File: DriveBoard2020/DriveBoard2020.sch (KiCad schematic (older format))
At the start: 51 parts

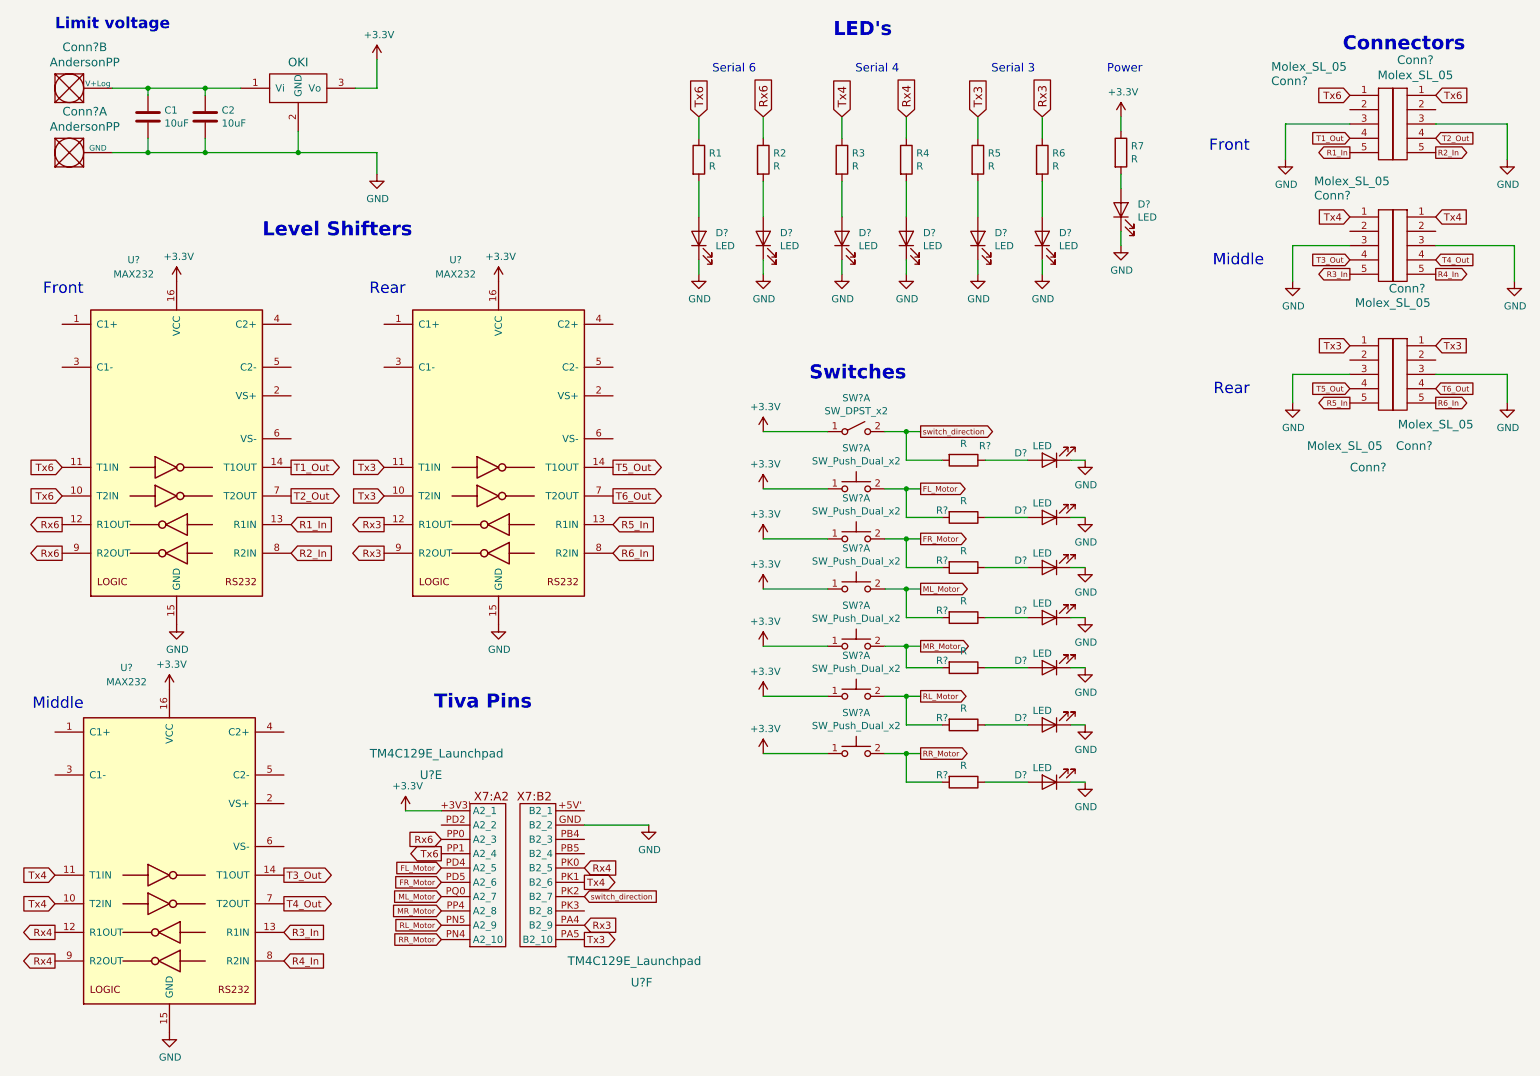
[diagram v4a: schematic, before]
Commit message: Cleaned up schematic, labled and added resistor values
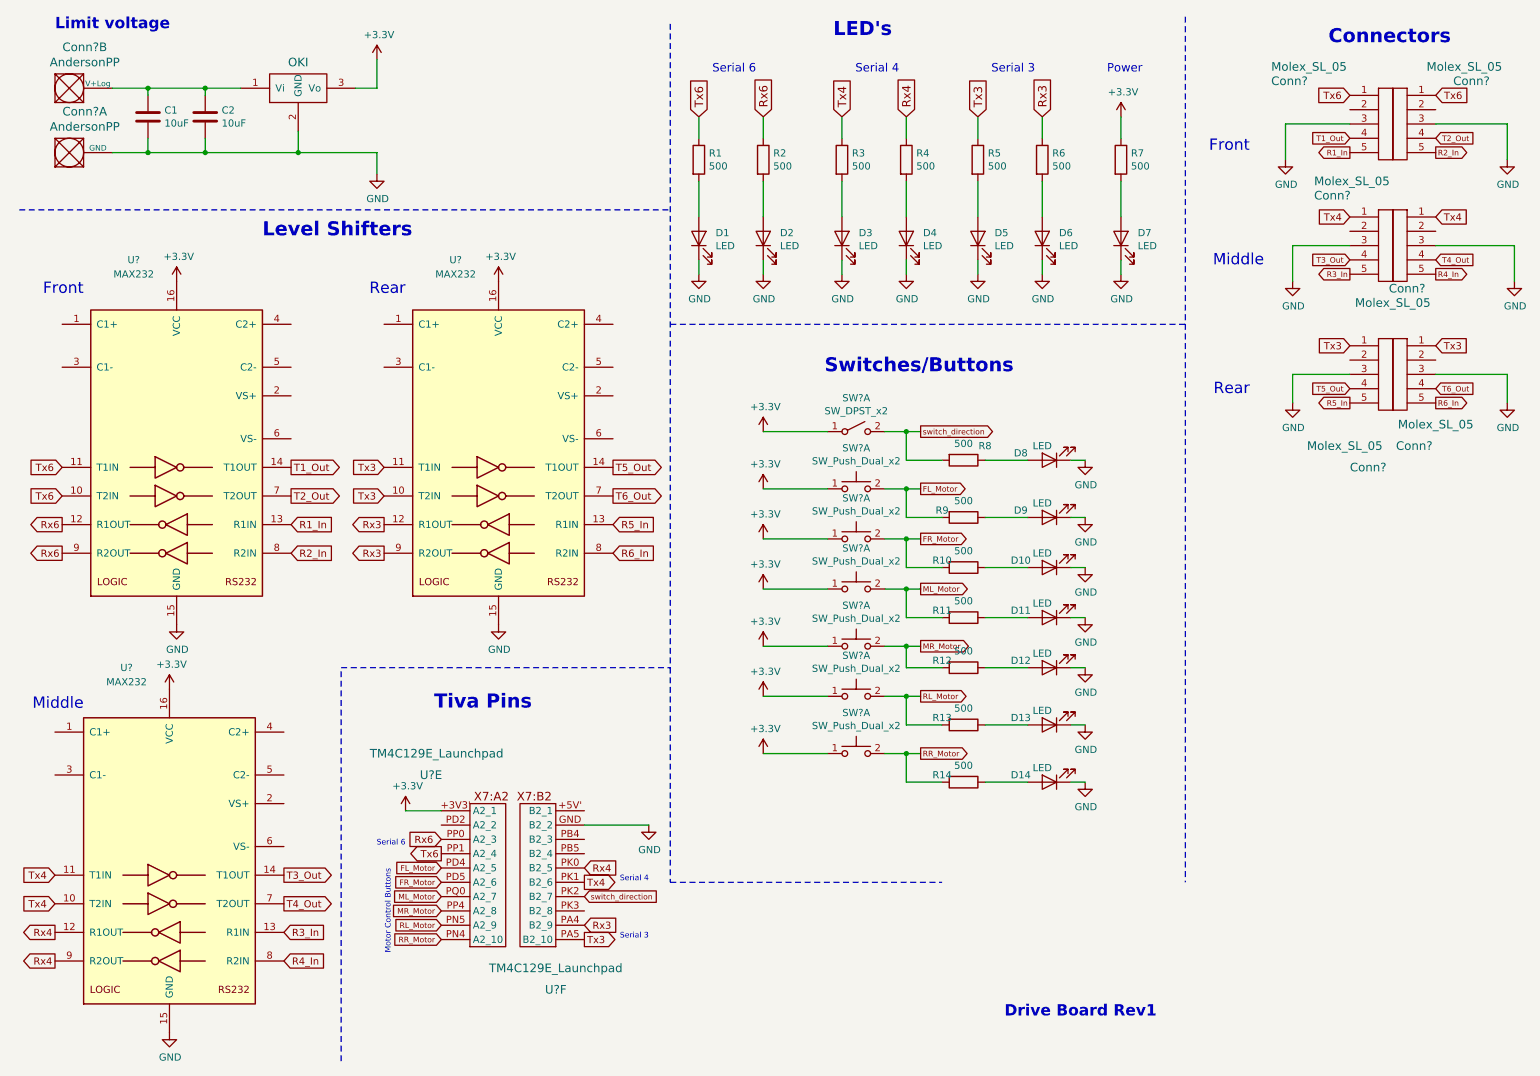
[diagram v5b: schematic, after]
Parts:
- R1, R2, R3, R4, R5, R6, R7: value R -> 500
- R10, R11, R12, R13, R14, R8, R9: renamed from R?; value R -> 500
- gave numbers to parts that had none: 14
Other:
- note added: "Drive Board Rev1"
- note added: "Motor Control Buttons"
- note added: "Switches/Buttons"
- note removed: "Switches"
- moved on the sheet: D7, R7
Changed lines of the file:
@@
 U 6 1 5D9A42ED
 P 4250 7000
-F 0 "U?" H 3650 6750 60  0000 C CNN
-F 1 "TM4C129E_Launchpad" H 3700 6900 60  0000 C CNN
+F 0 "U?" H 4250 6700 60  0000 C CNN
+F 1 "TM4C129E_Launchpad" H 4250 6850 60  0000 C CNN
 F 2 "" H 4250 7000 60  0001 C CNN
 F 3 "" H 4250 7000 60  0001 C CNN
@@
 U 1 1 5DA43D44
 P 10200 1500
-F 0 "Conn?" H 10142 2197 60  0000 C CNN
-F 1 "Molex_SL_05" H 10142 2091 60  0000 C CNN
+F 0 "Conn?" H 9750 2050 60  0000 C CNN
+F 1 "Molex_SL_05" H 9800 2150 60  0000 C CNN
 F 2 "" H 10200 1500 60  0001 C CNN
 F 3 "" H 10200 1500 60  0001 C CNN
@@
 Text GLabel 9800 1050 0    51   Input ~ 0
 Tx6
-Text Notes 9750 750  0    98   ~ 20
+Text Notes 9650 700  0    98   ~ 20
 Connectors
 $Comp
@@
 P 5250 1500
 F 0 "R1" H 5320 1546 50  0000 L CNN
-F 1 "R" H 5320 1455 50  0000 L CNN
+F 1 "500" H 5320 1455 50  0000 L CNN
 F 2 "" V 5180 1500 50  0001 C CNN
 F 3 "~" H 5250 1500 50  0001 C CNN
@@
 	5250 1650 5250 1900
 $Comp
-L Device:LED D?
+L Device:LED D1
 U 1 1 5DAADC37
 P 5250 2050
-F 0 "D?" V 5289 1933 50  0000 R CNN
+F 0 "D1" V 5289 1933 50  0000 R CNN
 F 1 "LED" V 5198 1933 50  0000 R CNN
 F 2 "" H 5250 2050 50  0001 C CNN
@@
 P 5700 1500
 F 0 "R2" H 5770 1546 50  0000 L CNN
-F 1 "R" H 5770 1455 50  0000 L CNN
+F 1 "500" H 5770 1455 50  0000 L CNN
 F 2 "" V 5630 1500 50  0001 C CNN
 F 3 "~" H 5700 1500 50  0001 C CNN
@@
 $EndComp
 $Comp
-L Device:LED D?
+L Device:LED D2
 U 1 1 5DAB09C5
 P 5700 2050
-F 0 "D?" V 5739 1933 50  0000 R CNN
+F 0 "D2" V 5739 1933 50  0000 R CNN
 F 1 "LED" V 5648 1933 50  0000 R CNN
 F 2 "" H 5700 2050 50  0001 C CNN
@@
 P 6250 1500
 F 0 "R3" H 6320 1546 50  0000 L CNN
-F 1 "R" H 6320 1455 50  0000 L CNN
+F 1 "500" H 6320 1455 50  0000 L CNN
 F 2 "" V 6180 1500 50  0001 C CNN
 F 3 "~" H 6250 1500 50  0001 C CNN
@@
 	6250 1650 6250 1900
 $Comp
-L Device:LED D?
+L Device:LED D3
 U 1 1 5DABA283
 P 6250 2050
-F 0 "D?" V 6289 1933 50  0000 R CNN
+F 0 "D3" V 6289 1933 50  0000 R CNN
 F 1 "LED" V 6198 1933 50  0000 R CNN
 F 2 "" H 6250 2050 50  0001 C CNN
@@
 P 6700 1500
 F 0 "R4" H 6770 1546 50  0000 L CNN
-F 1 "R" H 6770 1455 50  0000 L CNN
+F 1 "500" H 6770 1455 50  0000 L CNN
 F 2 "" V 6630 1500 50  0001 C CNN
 F 3 "~" H 6700 1500 50  0001 C CNN
@@
 $EndComp
 $Comp
-L Device:LED D?
+L Device:LED D4
 U 1 1 5DABA297
 P 6700 2050
-F 0 "D?" V 6739 1933 50  0000 R CNN
+F 0 "D4" V 6739 1933 50  0000 R CNN
 F 1 "LED" V 6648 1933 50  0000 R CNN
 F 2 "" H 6700 2050 50  0001 C CNN
@@
 P 7200 1500
 F 0 "R5" H 7270 1546 50  0000 L CNN
-F 1 "R" H 7270 1455 50  0000 L CNN
+F 1 "500" H 7270 1455 50  0000 L CNN
 F 2 "" V 7130 1500 50  0001 C CNN
 F 3 "~" H 7200 1500 50  0001 C CNN
@@
 	7200 1650 7200 1900
 $Comp
-L Device:LED D?
+L Device:LED D5
 U 1 1 5DABE1A4
 P 7200 2050
-F 0 "D?" V 7239 1933 50  0000 R CNN
+F 0 "D5" V 7239 1933 50  0000 R CNN
 F 1 "LED" V 7148 1933 50  0000 R CNN
 F 2 "" H 7200 2050 50  0001 C CNN
@@
 P 7650 1500
 F 0 "R6" H 7720 1546 50  0000 L CNN
-F 1 "R" H 7720 1455 50  0000 L CNN
+F 1 "500" H 7720 1455 50  0000 L CNN
 F 2 "" V 7580 1500 50  0001 C CNN
 F 3 "~" H 7650 1500 50  0001 C CNN
@@
 $EndComp
 $Comp
-L Device:LED D?
+L Device:LED D6
 U 1 1 5DABE1B8
 P 7650 2050
-F 0 "D?" V 7689 1933 50  0000 R CNN
+F 0 "D6" V 7689 1933 50  0000 R CNN
 F 1 "LED" V 7598 1933 50  0000 R CNN
 F 2 "" H 7650 2050 50  0001 C CNN
@@
 L Device:R R7
 U 1 1 5DAC01AD
-P 8200 1450
-F 0 "R7" H 8270 1496 50  0000 L CNN
-F 1 "R" H 8270 1405 50  0000 L CNN
-F 2 "" V 8130 1450 50  0001 C CNN
-F 3 "~" H 8200 1450 50  0001 C CNN
-	1    8200 1450
-	1    0    0    -1
-$EndComp
-Wire Wire Line
-	8200 1200 8200 1300
-$Comp
-L Device:LED D?
+P 8200 1500
+F 0 "R7" H 8270 1546 50  0000 L CNN
+F 1 "500" H 8270 1455 50  0000 L CNN
+F 2 "" V 8130 1500 50  0001 C CNN
+F 3 "~" H 8200 1500 50  0001 C CNN
+	1    8200 1500
+	1    0    0    -1
+$EndComp
+$Comp
+L Device:LED D7
 U 1 1 5DAC1A9F
-P 8200 1850
-F 0 "D?" V 8239 1733 50  0000 R CNN
-F 1 "LED" V 8148 1733 50  0000 R CNN
-F 2 "" H 8200 1850 50  0001 C CNN
-F 3 "~" H 8200 1850 50  0001 C CNN
-	1    8200 1850
+P 8200 2050
+F 0 "D7" V 8239 1933 50  0000 R CNN
+F 1 "LED" V 8148 1933 50  0000 R CNN
+F 2 "" H 8200 2050 50  0001 C CNN
+F 3 "~" H 8200 2050 50  0001 C CNN
+	1    8200 2050
 	0    -1   -1   0
 $EndComp
-Wire Wire Line
-	8200 1600 8200 1700
 $Comp
 L power:GND #PWR?
 U 1 1 5DAC3638
-P 8200 2100
-F 0 "#PWR?" H 8200 1850 50  0001 C CNN
-F 1 "GND" H 8205 1927 50  0000 C CNN
-F 2 "" H 8200 2100 50  0001 C CNN
-F 3 "" H 8200 2100 50  0001 C CNN
-	1    8200 2100
-	1    0    0    -1
-$EndComp
-Wire Wire Line
-	8200 2000 8200 2100
+P 8200 2300
+F 0 "#PWR?" H 8200 2050 50  0001 C CNN
+F 1 "GND" H 8205 2127 50  0000 C CNN
+F 2 "" H 8200 2300 50  0001 C CNN
+F 3 "" H 8200 2300 50  0001 C CNN
+	1    8200 2300
+	1    0    0    -1
+$EndComp
 Text Notes 8350 900  2    59   ~ 0
 Power
-Text Notes 6700 3050 2    98   ~ 20
-Switches
+Text Notes 7450 3000 2    98   ~ 20
+Switches/Buttons
 $Comp
 L Switch:SW_DPST_x2 SW?
@@
 	6700 3400 6800 3400
 $Comp
-L Device:LED D?
+L Device:LED D8
 U 1 1 5DB0DCCD
 P 7700 3600
-F 0 "D?" H 7900 3550 50  0000 C CNN
+F 0 "D8" H 7900 3550 50  0000 C CNN
 F 1 "LED" H 7750 3500 50  0000 C CNN
 F 2 "" H 7700 3600 50  0001 C CNN
@@
 $EndComp
 $Comp
-L Device:R R?
+L Device:R R8
 U 1 1 5DB0FB7A
 P 7100 3600
-F 0 "R?" V 7000 3750 50  0000 C CNN
-F 1 "R" V 6984 3600 50  0000 C CNN
+F 0 "R8" V 7000 3750 50  0000 C CNN
+F 1 "500" V 6984 3600 50  0000 C CNN
 F 2 "" V 7030 3600 50  0001 C CNN
 F 3 "~" H 7100 3600 50  0001 C CNN
@@
 	6700 3800 6800 3800
 $Comp
-L Device:R R?
+L Device:R R9
 U 1 1 5DB14CA8
 P 7100 4000
-F 0 "R?" V 7050 3850 50  0000 C CNN
-F 1 "R" V 6984 4000 50  0000 C CNN
+F 0 "R9" V 7050 3850 50  0000 C CNN
+F 1 "500" V 6984 4000 50  0000 C CNN
 F 2 "" V 7030 4000 50  0001 C CNN
 F 3 "~" H 7100 4000 50  0001 C CNN
@@
 	7250 4000 7550 4000
 $Comp
-L Device:LED D?
+L Device:LED D9
 U 1 1 5DB1AFB8
 P 7700 4000
-F 0 "D?" H 7900 3950 50  0000 C CNN
+F 0 "D9" H 7900 3950 50  0000 C CNN
 F 1 "LED" H 7750 3900 50  0000 C CNN
 F 2 "" H 7700 4000 50  0001 C CNN
@@
 	6700 4150 6800 4150
 $Comp
-L Device:R R?
+L Device:R R10
 U 1 1 5DB1F255
 P 7100 4350
-F 0 "R?" V 7050 4200 50  0000 C CNN
-F 1 "R" V 6984 4350 50  0000 C CNN
+F 0 "R10" V 7050 4200 50  0000 C CNN
+F 1 "500" V 6984 4350 50  0000 C CNN
 F 2 "" V 7030 4350 50  0001 C CNN
 F 3 "~" H 7100 4350 50  0001 C CNN
@@
 	7250 4350 7550 4350
 $Comp
-L Device:LED D?
+L Device:LED D10
 U 1 1 5DB21877
 P 7700 4350
-F 0 "D?" H 7900 4300 50  0000 C CNN
+F 0 "D10" H 7900 4300 50  0000 C CNN
 F 1 "LED" H 7750 4250 50  0000 C CNN
 F 2 "" H 7700 4350 50  0001 C CNN
@@
 	6700 4500 6800 4500
 $Comp
-L Device:R R?
+L Device:R R11
 U 1 1 5DB2408E
 P 7100 4700
-F 0 "R?" V 7050 4550 50  0000 C CNN
-F 1 "R" V 6984 4700 50  0000 C CNN
+F 0 "R11" V 7050 4550 50  0000 C CNN
+F 1 "500" V 6984 4700 50  0000 C CNN
 F 2 "" V 7030 4700 50  0001 C CNN
 F 3 "~" H 7100 4700 50  0001 C CNN
@@
 	7250 4700 7550 4700
 $Comp
-L Device:LED D?
+L Device:LED D11
 U 1 1 5DB26770
 P 7700 4700
-F 0 "D?" H 7900 4650 50  0000 C CNN
+F 0 "D11" H 7900 4650 50  0000 C CNN
 F 1 "LED" H 7750 4600 50  0000 C CNN
 F 2 "" H 7700 4700 50  0001 C CNN
@@
 	6700 4900 6800 4900
 $Comp
-L Device:R R?
+L Device:R R12
 U 1 1 5DB29413
 P 7100 5050
-F 0 "R?" V 7050 4900 50  0000 C CNN
-F 1 "R" V 6984 5050 50  0000 C CNN
+F 0 "R12" V 7050 4900 50  0000 C CNN
+F 1 "500" V 6984 5050 50  0000 C CNN
 F 2 "" V 7030 5050 50  0001 C CNN
 F 3 "~" H 7100 5050 50  0001 C CNN
@@
 	7250 5050 7550 5050
 $Comp
-L Device:LED D?
+L Device:LED D12
 U 1 1 5DB2BE6F
 P 7700 5050
-F 0 "D?" H 7900 5000 50  0000 C CNN
+F 0 "D12" H 7900 5000 50  0000 C CNN
 F 1 "LED" H 7750 4950 50  0000 C CNN
 F 2 "" H 7700 5050 50  0001 C CNN
@@
 	6700 5250 6800 5250
 $Comp
-L Device:R R?
+L Device:R R13
 U 1 1 5DB2EE1B
 P 7100 5450
-F 0 "R?" V 7050 5300 50  0000 C CNN
-F 1 "R" V 6984 5450 50  0000 C CNN
+F 0 "R13" V 7050 5300 50  0000 C CNN
+F 1 "500" V 6984 5450 50  0000 C CNN
 F 2 "" V 7030 5450 50  0001 C CNN
 F 3 "~" H 7100 5450 50  0001 C CNN
@@
 	7250 5450 7550 5450
 $Comp
-L Device:LED D?
+L Device:LED D13
 U 1 1 5DB31B65
 P 7700 5450
-F 0 "D?" H 7900 5400 50  0000 C CNN
+F 0 "D13" H 7900 5400 50  0000 C CNN
 F 1 "LED" H 7750 5350 50  0000 C CNN
 F 2 "" H 7700 5450 50  0001 C CNN
@@
 	6700 5650 6800 5650
 $Comp
-L Device:R R?
+L Device:R R14
 U 1 1 5DB353D4
 P 7100 5850
-F 0 "R?" V 7050 5700 50  0000 C CNN
-F 1 "R" V 6984 5850 50  0000 C CNN
+F 0 "R14" V 7050 5700 50  0000 C CNN
+F 1 "500" V 6984 5850 50  0000 C CNN
 F 2 "" V 7030 5850 50  0001 C CNN
 F 3 "~" H 7100 5850 50  0001 C CNN
@@
 	7250 5850 7550 5850
 $Comp
-L Device:LED D?
+L Device:LED D14
 U 1 1 5DB38360
 P 7700 5850
-F 0 "D?" H 7900 5800 50  0000 C CNN
+F 0 "D14" H 7900 5800 50  0000 C CNN
 F 1 "LED" H 7750 5750 50  0000 C CNN
 F 2 "" H 7700 5850 50  0001 C CNN
@@
 Text GLabel 3450 6950 0    39   Input ~ 0
 RR_Motor
+Text Notes 3200 6300 2    39   ~ 0
+Serial 6
+Text Notes 4900 6550 2    39   ~ 0
+Serial 4
+Text Notes 4900 6950 2    39   ~ 0
+Serial 3
+Text Notes 3100 7050 1    39   ~ 0
+Motor Control Buttons
+Wire Wire Line
+	8200 2200 8200 2300
+Wire Wire Line
+	8200 1200 8200 1350
+Wire Wire Line
+	8200 1650 8200 1900
+Text Notes 8450 7500 2    79   ~ 16
+Drive Board Rev1
+Wire Notes Line style solid
+	2750 7800 2750 5050
+Wire Notes Line style solid
+	2750 5050 5050 5050
+Wire Notes Line style solid
+	500  1850 5050 1850
+Wire Notes Line style solid
+	5050 550  5050 5050
+Wire Notes Line style solid
+	5050 2650 8650 2650
+Wire Notes Line style solid
+	5050 5050 5050 6550
+Wire Notes Line style solid
+	5050 6550 6950 6550
+Wire Notes Line style solid
+	8650 500  8650 6550
 $EndSCHEMATC

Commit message: started assigning footprints
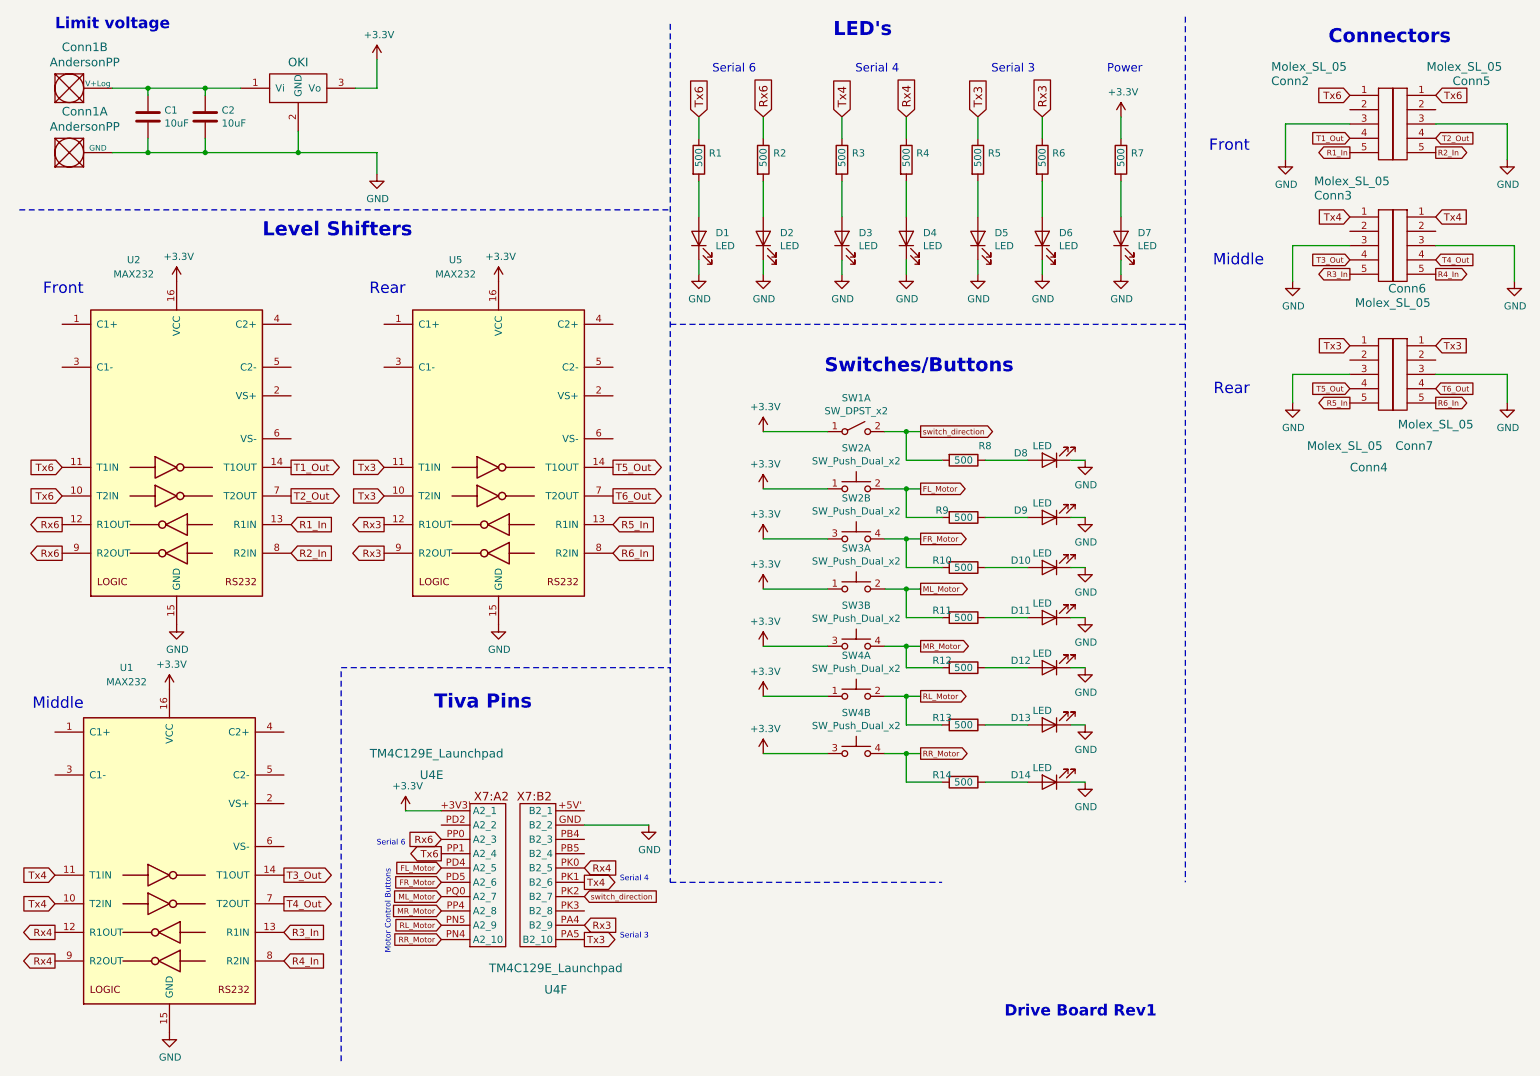
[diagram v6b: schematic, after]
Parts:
- C1, C2: footprint (none) -> Capacitor_SMD:C_0603_1608Metric_Pad1.05x0.95mm_HandSolder
- Conn1: renamed from Conn?; footprint (none) -> MRDT_Connectors:Anderson_2_Horizontal_Side_by_Side
- Conn2, Conn3, Conn4, Conn5, Conn6, Conn7: renamed from Conn?; footprint (none) -> MRDT_Connectors:MOLEX_SL_05_Horizontal
- D1, D10, D11, D12, D13, D14, D2, D3, D4, D5, D6, D7, D8, D9: footprint (none) -> LED_SMD:LED_0603_1608Metric_Pad1.05x0.95mm_HandSolder
- R1, R10, R11, R12, R13, R14, R2, R3, R4, R5, R6, R7, R8, R9: footprint (none) -> Resistor_SMD:R_0603_1608Metric_Pad1.05x0.95mm_HandSolder
- U3: renamed from U?; footprint (none) -> MRDT_Devices:OKI_Horizontal
- gave numbers to parts that had none: 8
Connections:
- net +3V3: now also SW2.3 (C), SW3.3 (C), SW4.3 (C); no longer SW2.1 (C), SW3.1 (C), SW4.1 (C)
- net FR_Motor: now also SW2.4 (D); no longer SW2.2 (D)
- net MR_Motor: now also SW3.4 (D); no longer SW3.2 (D)
- net RR_Motor: now also SW4.4 (D); no longer SW4.2 (D)
